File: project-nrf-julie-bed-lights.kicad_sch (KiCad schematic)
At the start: 30 parts

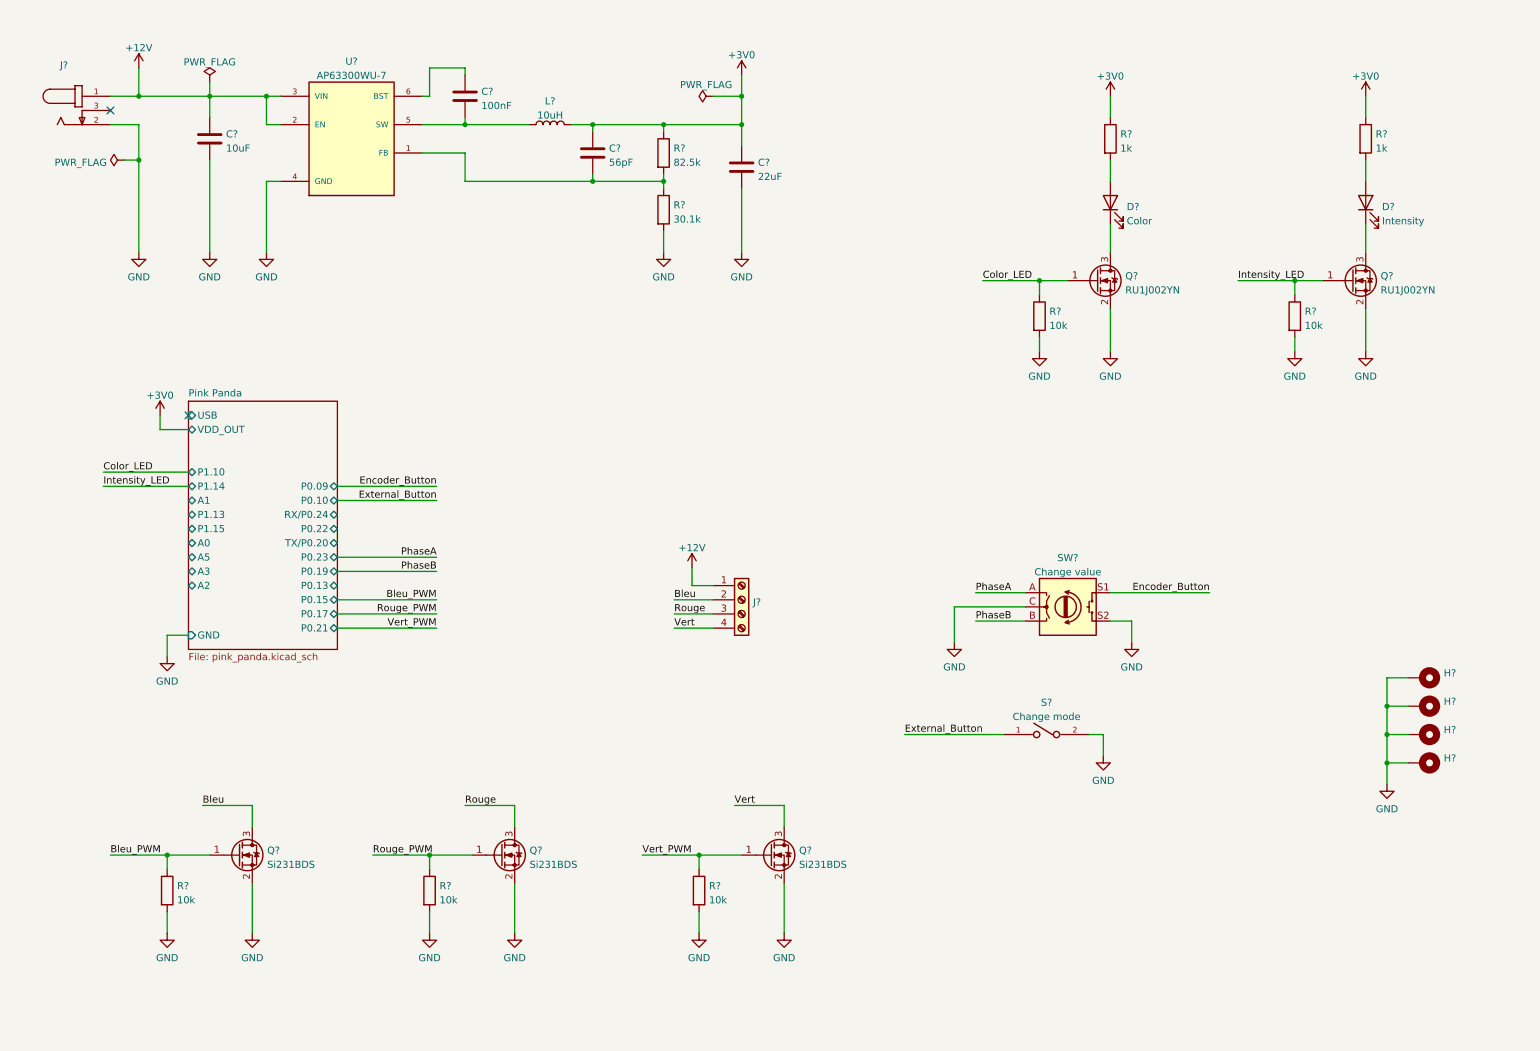
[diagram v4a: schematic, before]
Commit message: Add an ap63300 sheet
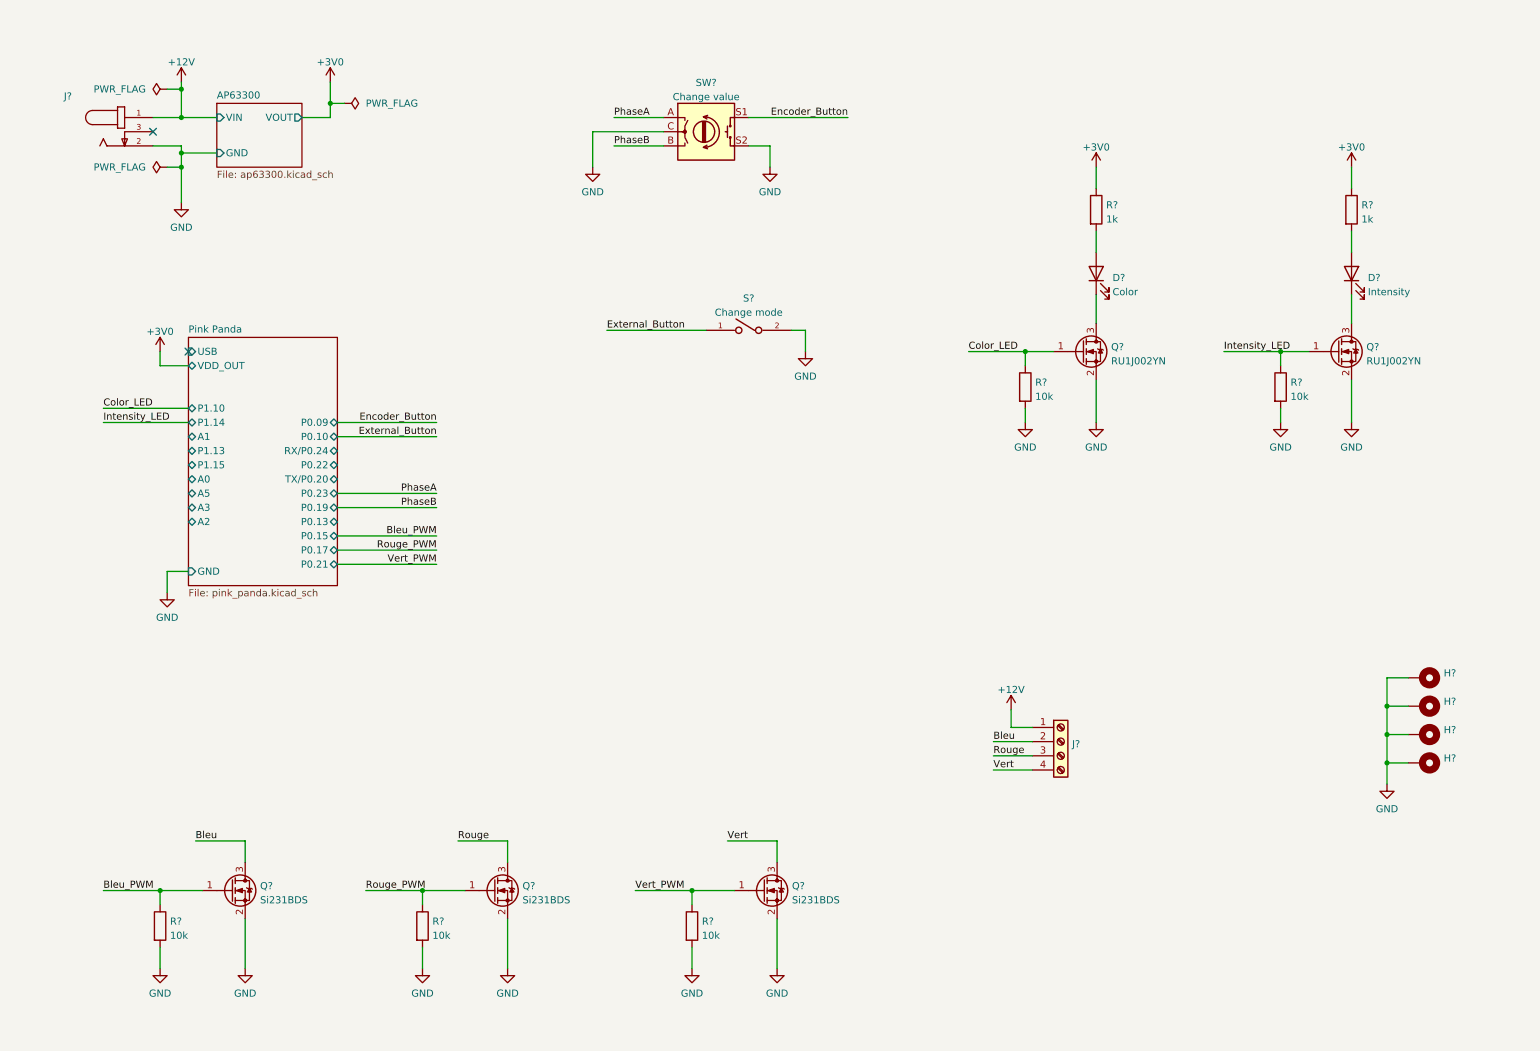
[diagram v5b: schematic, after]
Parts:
- removed C?: 100nF, Capacitor_SMD:C_0603_1608Metric, symbol Device:C
- removed C?: 10uF, Capacitor_SMD:C_0805_2012Metric, symbol Device:C
- removed C?: 22uF, Capacitor_SMD:C_0805_2012Metric, symbol Device:C
- removed C?: 56pF, Capacitor_SMD:C_0603_1608Metric, symbol Device:C
- removed L?: 10uH, LBR2518T100K:INDC2518X200N, symbol LBR2518T100K:LBR2518T100K
- removed R?: 30.1k, Resistor_SMD:R_0603_1608Metric, symbol Device:R
- removed R?: 82.5k, Resistor_SMD:R_0603_1608Metric, symbol Device:R
- removed U?: AP63300WU-7, AP63300WU-7:SOT95P280X100-6N, symbol AP63300WU-7:AP63300WU-7
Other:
- added sheet AP63300 (ap63300.kicad_sch)
- moved on the sheet: D?, J?, Q?, R?, S?, SW?

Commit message: Add separations in main sheet
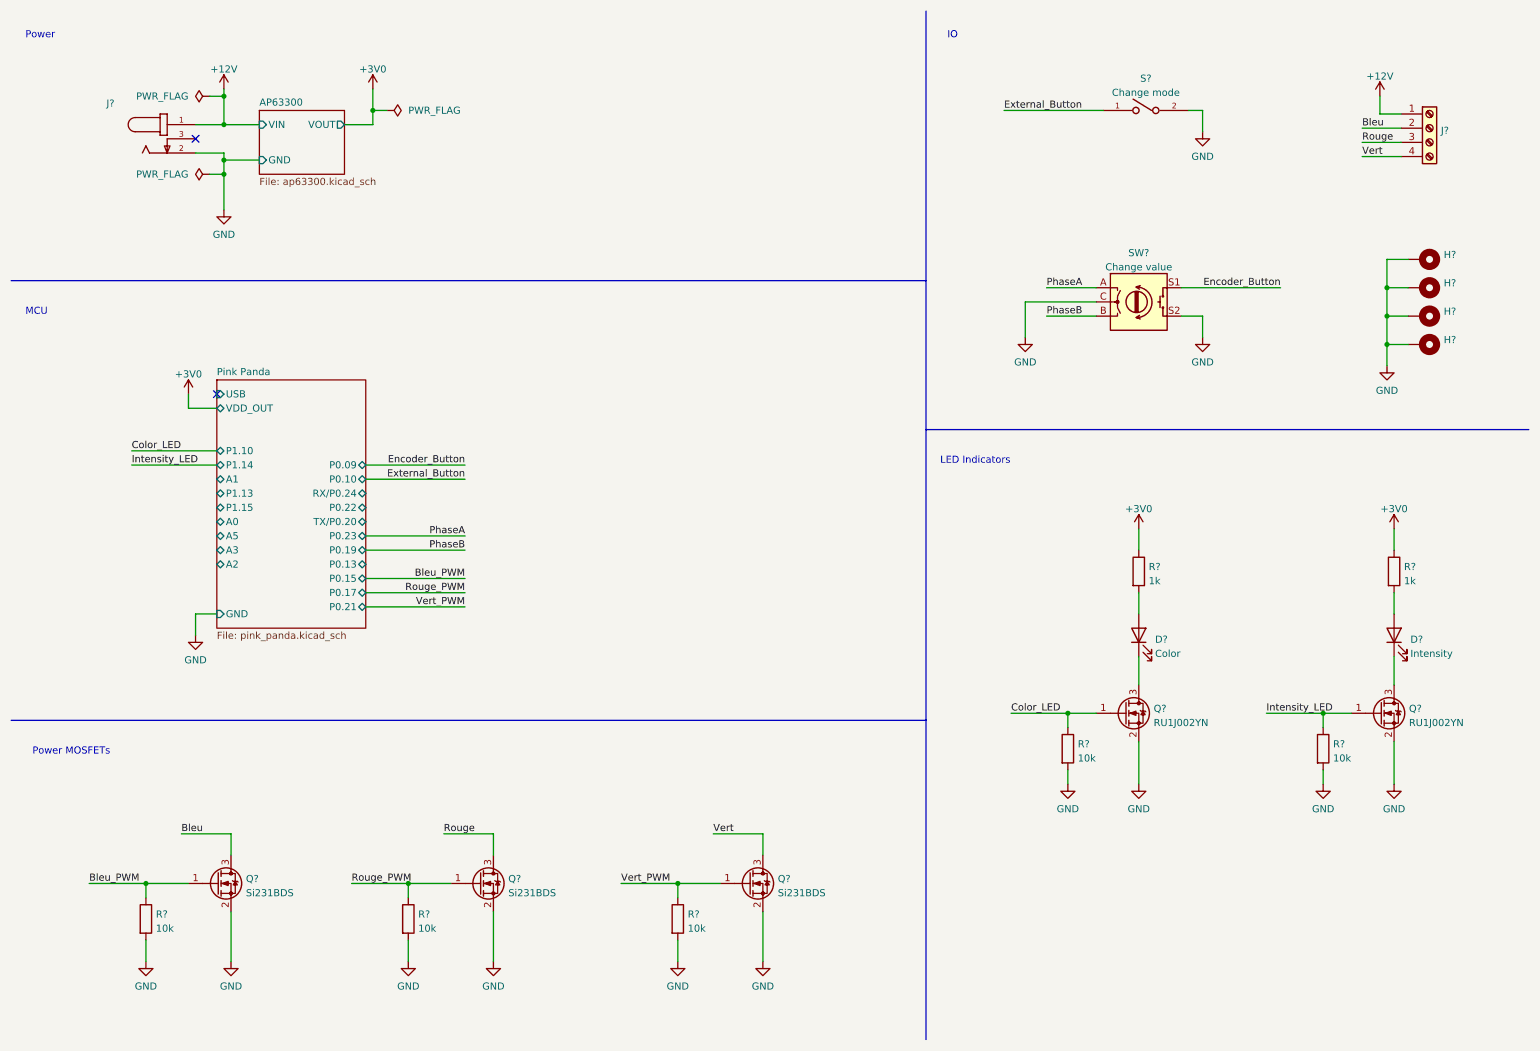
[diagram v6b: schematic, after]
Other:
- note added: "IO"
- note added: "LED Indicators"
- note added: "MCU"
- note added: "Power"
- note added: "Power MOSFETs"
- moved on the sheet: D?, H?, J?, Q?, R?, S?, SW?
